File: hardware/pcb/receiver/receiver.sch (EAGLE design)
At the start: 78 parts, among them X1 5-1634506-1H

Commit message: hw: order list, receiver board schematic
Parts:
- added H1, H2, H3, H4: MOUNT-HOLE3.3, holes:MOUNT-HOLE3.3
- R7, R8, R9: MFR RC0805FR-0710KLRC0805FR-0710KL -> RC0805FR-0710KL
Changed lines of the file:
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@@
 <?xml version="1.0" encoding="utf-8"?>
 <!DOCTYPE eagle SYSTEM "eagle.dtd">
-<eagle version="7.5.0">
+<eagle version="7.3.0">
 <drawing>
 <settings>
@@
 <grid distance="0.1" unitdist="inch" unit="inch" style="lines" multiple="1" display="yes" altdistance="0.01" altunitdist="inch" altunit="inch"/>
 <layers>
-<layer number="1" name="Top" color="4" fill="1" visible="yes" active="no"/>
-<layer number="16" name="Bottom" color="1" fill="1" visible="yes" active="no"/>
-<layer number="17" name="Pads" color="2" fill="1" visible="yes" active="no"/>
-<layer number="18" name="Vias" color="2" fill="1" visible="yes" active="no"/>
-<layer number="19" name="Unrouted" color="6" fill="1" visible="yes" active="no"/>
-<layer number="20" name="Dimension" color="15" fill="1" visible="yes" active="no"/>
-<layer number="21" name="tPlace" color="7" fill="1" visible="yes" active="no"/>
-<layer number="22" name="bPlace" color="7" fill="1" visible="yes" active="no"/>
-<layer number="23" name="tOrigins" color="15" fill="1" visible="yes" active="no"/>
-<layer number="24" name="bOrigins" color="15" fill="1" visible="yes" active="no"/>
-<layer number="25" name="tNames" color="7" fill="1" visible="yes" active="no"/>
-<layer number="26" name="bNames" color="7" fill="1" visible="yes" active="no"/>
-<layer number="27" name="tValues" color="7" fill="1" visible="yes" active="no"/>
-<layer number="28" name="bValues" color="7" fill="1" visible="yes" active="no"/>
+<layer number="1" name="Top" color="4" fill="1" visible="no" active="no"/>
+<layer number="2" name="Route2" color="1" fill="3" visible="no" active="no"/>
+<layer number="3" name="Route3" color="4" fill="3" visible="no" active="no"/>
+<layer number="4" name="Route4" color="1" fill="4" visible="no" active="no"/>
+<layer number="5" name="Route5" color="4" fill="4" visible="no" active="no"/>
+<layer number="6" name="Route6" color="1" fill="8" visible="no" active="no"/>
+<layer number="7" name="Route7" color="4" fill="8" visible="no" active="no"/>
+<layer number="8" name="Route8" color="1" fill="2" visible="no" active="no"/>
+<layer number="9" name="Route9" color="4" fill="2" visible="no" active="no"/>
+<layer number="10" name="Route10" color="1" fill="7" visible="no" active="no"/>
+<layer number="11" name="Route11" color="4" fill="7" visible="no" active="no"/>
+<layer number="12" name="Route12" color="1" fill="5" visible="no" active="no"/>
+<layer number="13" name="Route13" color="4" fill="5" visible="no" active="no"/>
+<layer number="14" name="Route14" color="1" fill="6" visible="no" active="no"/>
+<layer number="15" name="Route15" color="4" fill="6" visible="no" active="no"/>
+<layer number="16" name="Bottom" color="1" fill="1" visible="no" active="no"/>
+<layer number="17" name="Pads" color="2" fill="1" visible="no" active="no"/>
+<layer number="18" name="Vias" color="2" fill="1" visible="no" active="no"/>
+<layer number="19" name="Unrouted" color="6" fill="1" visible="no" active="no"/>
+<layer number="20" name="Dimension" color="15" fill="1" visible="no" active="no"/>
+<layer number="21" name="tPlace" color="7" fill="1" visible="no" active="no"/>
+<layer number="22" name="bPlace" color="7" fill="1" visible="no" active="no"/>
+<layer number="23" name="tOrigins" color="15" fill="1" visible="no" active="no"/>
+<layer number="24" name="bOrigins" color="15" fill="1" visible="no" active="no"/>
+<layer number="25" name="tNames" color="7" fill="1" visible="no" active="no"/>
+<layer number="26" name="bNames" color="7" fill="1" visible="no" active="no"/>
+<layer number="27" name="tValues" color="7" fill="1" visible="no" active="no"/>
+<layer number="28" name="bValues" color="7" fill="1" visible="no" active="no"/>
 <layer number="29" name="tStop" color="7" fill="3" visible="no" active="no"/>
 <layer number="30" name="bStop" color="7" fill="6" visible="no" active="no"/>
@@
 <layer number="35" name="tGlue" color="7" fill="4" visible="no" active="no"/>
 <layer number="36" name="bGlue" color="7" fill="5" visible="no" active="no"/>
-<layer number="37" name="tTest" color="7" fill="1" visible="yes" active="no"/>
-<layer number="38" name="bTest" color="7" fill="1" visible="yes" active="no"/>
+<layer number="37" name="tTest" color="7" fill="1" visible="no" active="no"/>
+<layer number="38" name="bTest" color="7" fill="1" visible="no" active="no"/>
 <layer number="39" name="tKeepout" color="4" fill="11" visible="no" active="no"/>
 <layer number="40" name="bKeepout" color="1" fill="11" visible="no" active="no"/>
@@
 <layer number="44" name="Drills" color="7" fill="1" visible="no" active="no"/>
 <layer number="45" name="Holes" color="7" fill="1" visible="no" active="no"/>
-<layer number="46" name="Milling" color="3" fill="1" visible="yes" active="no"/>
-<layer number="47" name="Measures" color="7" fill="1" visible="yes" active="no"/>
-<layer number="48" name="Document" color="7" fill="1" visible="yes" active="no"/>
-<layer number="49" name="Reference" color="7" fill="1" visible="yes" active="no"/>
-<layer number="50" name="dxf" color="7" fill="1" visible="yes" active="no"/>
-<layer number="51" name="tDocu" color="7" fill="1" visible="yes" active="no"/>
-<layer number="52" name="bDocu" color="7" fill="1" visible="yes" active="no"/>
-<layer number="53" name="tGND_GNDA" color="7" fill="9" visible="yes" active="no"/>
-<layer number="54" name="bGND_GNDA" color="1" fill="9" visible="yes" active="no"/>
-<layer number="56" name="wert" color="7" fill="1" visible="yes" active="no"/>
-<layer number="57" name="tCAD" color="7" fill="1" visible="yes" active="no"/>
-<layer number="59" name="tCarbon" color="7" fill="1" visible="yes" active="no"/>
-<layer number="60" name="bCarbon" color="7" fill="1" visible="yes" active="no"/>
+<layer number="46" name="Milling" color="3" fill="1" visible="no" active="no"/>
+<layer number="47" name="Measures" color="7" fill="1" visible="no" active="no"/>
+<layer number="48" name="Document" color="7" fill="1" visible="no" active="no"/>
+<layer number="49" name="Reference" color="7" fill="1" visible="no" active="no"/>
+<layer number="50" name="dxf" color="7" fill="1" visible="no" active="no"/>
+<layer number="51" name="tDocu" color="7" fill="1" visible="no" active="no"/>
+<layer number="52" name="bDocu" color="7" fill="1" visible="no" active="no"/>
+<layer number="53" name="tGND_GNDA" color="7" fill="9" visible="no" active="no"/>
+<layer number="54" name="bGND_GNDA" color="1" fill="9" visible="no" active="no"/>
+<layer number="56" name="wert" color="7" fill="1" visible="no" active="no"/>
+<layer number="57" name="tCAD" color="7" fill="1" visible="no" active="no"/>
+<layer number="59" name="tCarbon" color="7" fill="1" visible="no" active="no"/>
+<layer number="60" name="bCarbon" color="7" fill="1" visible="no" active="no"/>
 <layer number="90" name="Modules" color="5" fill="1" visible="yes" active="yes"/>
 <layer number="91" name="Nets" color="2" fill="1" visible="yes" active="yes"/>
@@
 <part name="+3V5" library="supply1" deviceset="+3V3" device=""/>
 <part name="R7" library="rcl" deviceset="R-EU_" device="M0805" value="10k">
-<attribute name="MFR" value="RC0805FR-0710KLRC0805FR-0710KL"/>
+<attribute name="MFR" value="RC0805FR-0710KL"/>
 </part>
 <part name="JP1" library="lstolcman_thesis" deviceset="PINHD-2X4" device="">
@@
 </part>
 <part name="R8" library="rcl" deviceset="R-EU_" device="M0805" value="10k">
-<attribute name="MFR" value="RC0805FR-0710KLRC0805FR-0710KL"/>
+<attribute name="MFR" value="RC0805FR-0710KL"/>
 </part>
 <part name="R9" library="rcl" deviceset="R-EU_" device="M0805" value="10k">
-<attribute name="MFR" value="RC0805FR-0710KLRC0805FR-0710KL"/>
+<attribute name="MFR" value="RC0805FR-0710KL"/>
 </part>
 <part name="R12" library="rcl" deviceset="R-EU_" device="M0805" value="130R">
@@
 <attribute name="MFR" value="5-1634506-1"/>
 </part>
+<part name="H1" library="holes" deviceset="MOUNT-HOLE" device="3.3"/>
+<part name="H2" library="holes" deviceset="MOUNT-HOLE" device="3.3"/>
+<part name="H3" library="holes" deviceset="MOUNT-HOLE" device="3.3"/>
+<part name="H4" library="holes" deviceset="MOUNT-HOLE" device="3.3"/>
 </parts>
 <sheets>
@@
 <attribute name="MFR" x="-342.9" y="63.5" size="1.778" layer="96" display="off"/>
 </instance>
+<instance part="H1" gate="G$1" x="-340.36" y="10.16"/>
+<instance part="H2" gate="G$1" x="-340.36" y="2.54"/>
+<instance part="H3" gate="G$1" x="-340.36" y="-5.08"/>
+<instance part="H4" gate="G$1" x="-340.36" y="-12.7"/>
 </instances>
 <busses>

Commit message: hw: receiver board changes
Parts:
- removed C17, C23: 100n, rcl:C-EUC0805
- removed L6: ferrite bead, inductor-neosid:SM-NE29
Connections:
- removed net N$35: SV1.GPIO_00
- net +3V3: no longer C17.2, C42.2, JP1.1, L6.2, R11.2, R12.2, R7.2, V1.VCC
- net +3V3A_ADC: now also JP1.1, R11.2, R12.2, R7.2; no longer C23.2
- net AMPOUT_N: now also IC2.+OUT, R2.1; no longer IC2.-OUT, R1.1
- net AMPOUT_P: now also IC2.-OUT, R1.1; no longer IC2.+OUT, R2.1
- net ENC: now also SV1.GPIO_00; no longer SV1.GPIO_05
- net ENC_N: now also IC5.ENC_P; no longer IC5.ENC_N
- net ENC_P: now also IC5.ENC_N; no longer IC5.ENC_P
- net GND: no longer C17.1, C23.1
- net IN_N: now also IC5.AIN_N, R2.2; no longer IC5.AIN_P, R1.2
- net IN_P: now also IC5.AIN_P, R1.2; no longer IC5.AIN_N, R2.2
- net N$4: now also IC2.+IN; no longer IC2.-IN
- net N$5: now also IC2.-IN; no longer IC2.+IN
- net VDD: now also C42.2, V1.VCC; no longer L6.1
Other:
- moved on the sheet: C3, C38, C4, C5, R1, R2

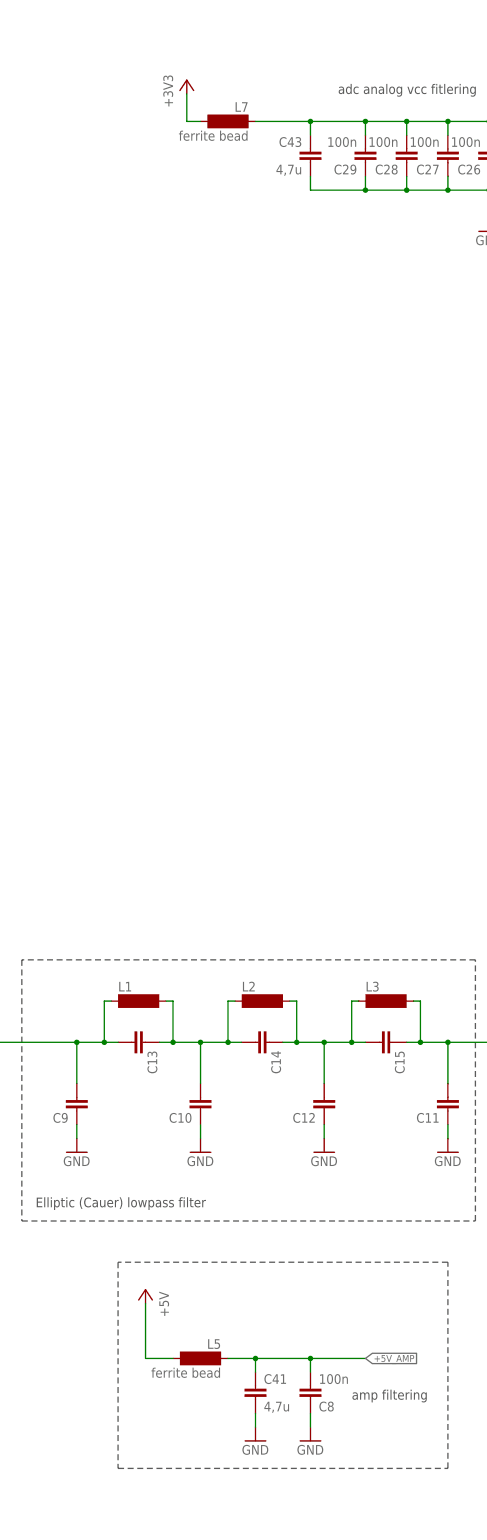
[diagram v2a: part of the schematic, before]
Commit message: hw: receiver ferrite beads between capacitors
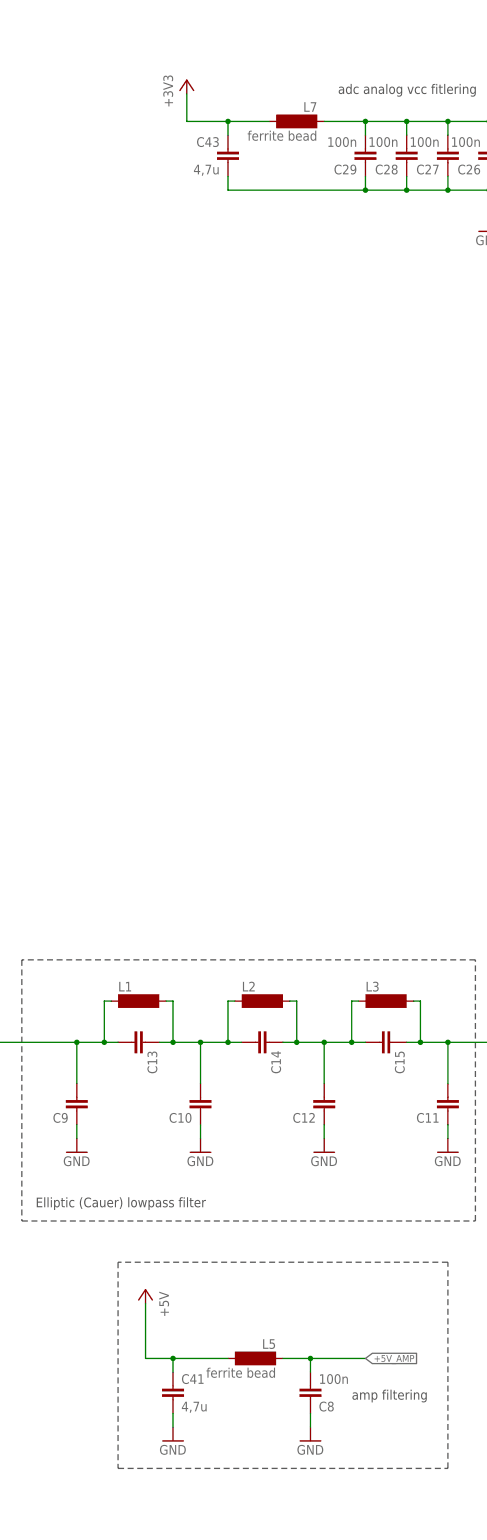
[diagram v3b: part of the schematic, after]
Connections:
- net +3V3: now also C43.1
- net +3V3A_ADC: no longer C43.1
- net +5V: now also C41.1
- net +5V_AMP: no longer C41.1
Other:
- moved on the sheet: C41, C43, L5, L7
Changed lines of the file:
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@@
 </instance>
 <instance part="GND19" gate="1" x="78.74" y="33.02"/>
-<instance part="L7" gate="G$1" x="-248.92" y="233.68" rot="MR0">
-<attribute name="MFR" x="-248.92" y="233.68" size="1.778" layer="96" rot="MR0" display="off"/>
+<instance part="L7" gate="G$1" x="-236.22" y="233.68" rot="MR0">
+<attribute name="MFR" x="-236.22" y="233.68" size="1.778" layer="96" rot="MR0" display="off"/>
 </instance>
 <instance part="C33" gate="G$1" x="147.32" y="43.18">
@@
 <attribute name="MFR" x="-53.34" y="223.52" size="1.778" layer="96" rot="MR0" display="off"/>
 </instance>
-<instance part="L5" gate="G$1" x="-254" y="5.08" rot="MR0">
-<attribute name="MFR" x="-254" y="5.08" size="1.778" layer="96" rot="MR0" display="off"/>
+<instance part="L5" gate="G$1" x="-243.84" y="5.08" rot="MR0">
+<attribute name="MFR" x="-243.84" y="5.08" size="1.778" layer="96" rot="MR0" display="off"/>
 </instance>
 <instance part="C34" gate="G$1" x="-233.68" y="276.86">
@@
 <attribute name="MFR" x="-109.22" y="213.36" size="2.54" layer="96" display="off"/>
 </instance>
-<instance part="C41" gate="G$1" x="-243.84" y="0">
-<attribute name="MFR" x="-243.84" y="0" size="2.54" layer="96" display="off"/>
-</instance>
-<instance part="GND31" gate="1" x="-243.84" y="-10.16"/>
+<instance part="C41" gate="G$1" x="-259.08" y="0">
+<attribute name="MFR" x="-259.08" y="0" size="2.54" layer="96" display="off"/>
+</instance>
+<instance part="GND31" gate="1" x="-259.08" y="-10.16"/>
 <instance part="C42" gate="G$1" x="73.66" y="-15.24" rot="R180">
 <attribute name="MFR" x="73.66" y="-15.24" size="2.54" layer="96" rot="R180" display="off"/>
@@
 <instance part="GND32" gate="1" x="73.66" y="-22.86"/>
 <instance part="+3V4" gate="G$1" x="-256.54" y="241.3"/>
-<instance part="C43" gate="G$1" x="-233.68" y="228.6" rot="MR0">
-<attribute name="MFR" x="-233.68" y="228.6" size="2.54" layer="96" rot="MR0" display="off"/>
+<instance part="C43" gate="G$1" x="-248.92" y="228.6" rot="MR0">
+<attribute name="MFR" x="-248.92" y="228.6" size="2.54" layer="96" rot="MR0" display="off"/>
 </instance>
 <instance part="+3V1" gate="G$1" x="-43.18" y="233.68"/>
@@
 <pinref part="C29" gate="G$1" pin="1"/>
 <pinref part="C43" gate="G$1" pin="2"/>
-<wire x1="-233.68" y1="220.98" x2="-233.68" y2="223.52" width="0.1524" layer="91"/>
-<wire x1="-233.68" y1="220.98" x2="-223.52" y2="220.98" width="0.1524" layer="91"/>
+<wire x1="-223.52" y1="220.98" x2="-248.92" y2="220.98" width="0.1524" layer="91"/>
+<wire x1="-248.92" y1="220.98" x2="-248.92" y2="223.52" width="0.1524" layer="91"/>
 <junction x="-223.52" y="220.98"/>
 </segment>
@@
 <segment>
 <pinref part="C41" gate="G$1" pin="2"/>
-<wire x1="-243.84" y1="-5.08" x2="-243.84" y2="-7.62" width="0.1524" layer="91"/>
+<wire x1="-259.08" y1="-5.08" x2="-259.08" y2="-7.62" width="0.1524" layer="91"/>
 <pinref part="GND31" gate="1" pin="GND"/>
 </segment>
@@
 <segment>
 <pinref part="L7" gate="G$1" pin="2"/>
-<wire x1="-254" y1="233.68" x2="-256.54" y2="233.68" width="0.1524" layer="91"/>
+<wire x1="-241.3" y1="233.68" x2="-248.92" y2="233.68" width="0.1524" layer="91"/>
+<wire x1="-248.92" y1="233.68" x2="-256.54" y2="233.68" width="0.1524" layer="91"/>
 <wire x1="-256.54" y1="233.68" x2="-256.54" y2="238.76" width="0.1524" layer="91"/>
 <pinref part="+3V4" gate="G$1" pin="+3V3"/>
+<pinref part="C43" gate="G$1" pin="1"/>
+<wire x1="-248.92" y1="231.14" x2="-248.92" y2="233.68" width="0.1524" layer="91"/>
+<junction x="-248.92" y="233.68"/>
 </segment>
 </net>
@@
 <pinref part="C29" gate="G$1" pin="2"/>
 <pinref part="L7" gate="G$1" pin="1"/>
-<wire x1="-223.52" y1="233.68" x2="-233.68" y2="233.68" width="0.1524" layer="91"/>
-<wire x1="-233.68" y1="233.68" x2="-243.84" y2="233.68" width="0.1524" layer="91"/>
+<wire x1="-223.52" y1="233.68" x2="-231.14" y2="233.68" width="0.1524" layer="91"/>
 <junction x="-223.52" y="233.68"/>
-<pinref part="C43" gate="G$1" pin="1"/>
-<wire x1="-233.68" y1="231.14" x2="-233.68" y2="233.68" width="0.1524" layer="91"/>
-<junction x="-233.68" y="233.68"/>
 <wire x1="-200.66" y1="233.68" x2="-200.66" y2="238.76" width="0.1524" layer="91"/>
 <wire x1="-200.66" y1="238.76" x2="-193.04" y2="238.76" width="0.1524" layer="91"/>
@@
 <net name="+5V_AMP" class="0">
 <segment>
-<wire x1="-248.92" y1="5.08" x2="-243.84" y2="5.08" width="0.1524" layer="91"/>
 <label x="-223.52" y="5.08" size="1.27" layer="95" xref="yes"/>
-<wire x1="-243.84" y1="5.08" x2="-233.68" y2="5.08" width="0.1524" layer="91"/>
+<wire x1="-238.76" y1="5.08" x2="-233.68" y2="5.08" width="0.1524" layer="91"/>
 <wire x1="-233.68" y1="5.08" x2="-223.52" y2="5.08" width="0.1524" layer="91"/>
 <wire x1="-233.68" y1="2.54" x2="-233.68" y2="5.08" width="0.1524" layer="91"/>
@@
 <pinref part="C8" gate="G$1" pin="2"/>
 <pinref part="L5" gate="G$1" pin="1"/>
-<pinref part="C41" gate="G$1" pin="1"/>
-<wire x1="-243.84" y1="2.54" x2="-243.84" y2="5.08" width="0.1524" layer="91"/>
-<junction x="-243.84" y="5.08"/>
 </segment>
 <segment>
@@
 <wire x1="-264.16" y1="5.08" x2="-264.16" y2="15.24" width="0.1524" layer="91"/>
 <pinref part="P+1" gate="1" pin="+5V"/>
+<wire x1="-248.92" y1="5.08" x2="-259.08" y2="5.08" width="0.1524" layer="91"/>
+<pinref part="L5" gate="G$1" pin="2"/>
+<pinref part="C41" gate="G$1" pin="1"/>
 <wire x1="-259.08" y1="5.08" x2="-264.16" y2="5.08" width="0.1524" layer="91"/>
-<pinref part="L5" gate="G$1" pin="2"/>
-</segment>
-</net>
+<wire x1="-259.08" y1="2.54" x2="-259.08" y2="5.08" width="0.1524" layer="91"/>
+<junction x="-259.08" y="5.08"/>
+</segment>
+</net>

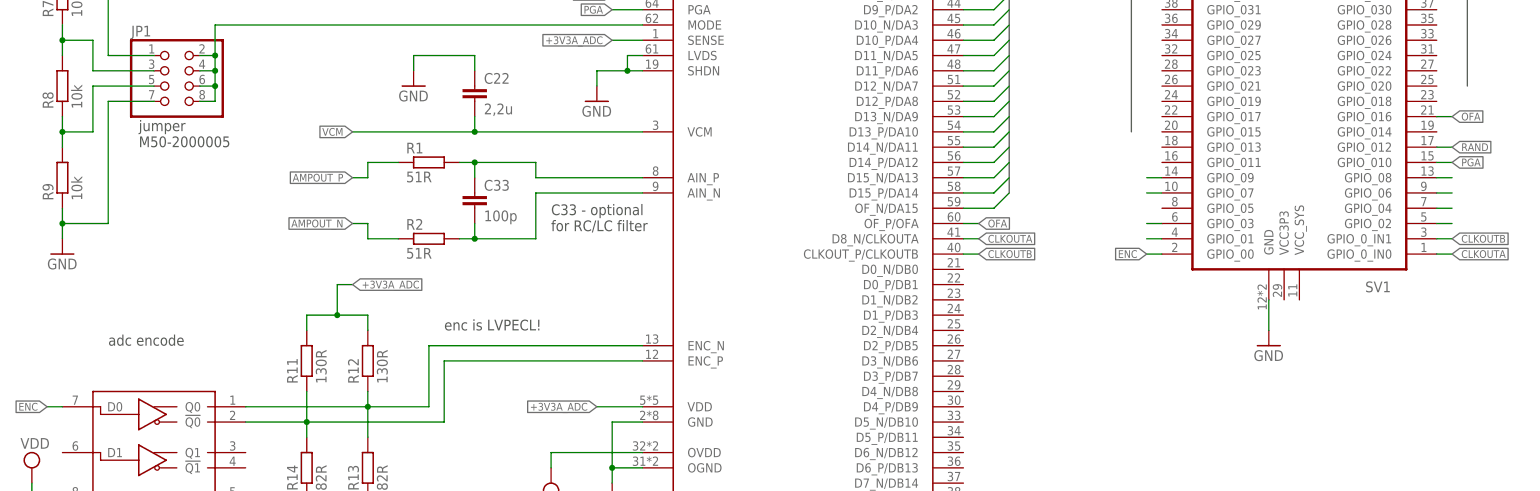
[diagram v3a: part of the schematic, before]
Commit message: hw: modified adc input clock resistors resistors
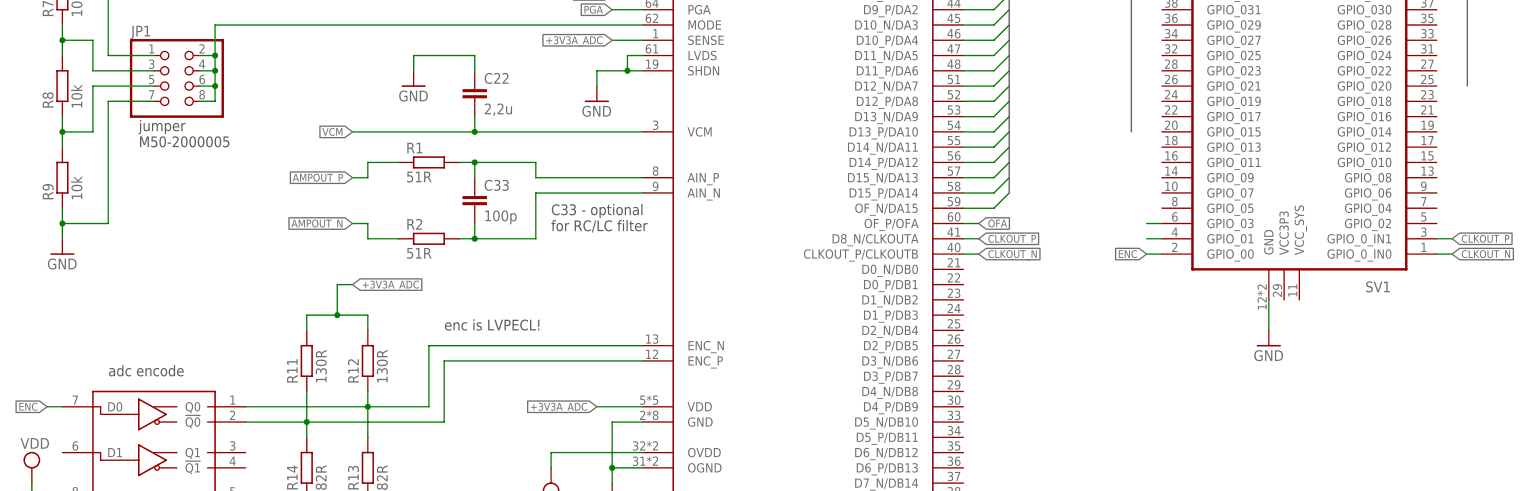
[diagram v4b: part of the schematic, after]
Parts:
- R11, R12: device rcl:R-EU_M0805 -> rcl:R-EU_M1206; MFR RC0805FR-07130RL -> ERJ-8ENF1300V
- R13, R14: device rcl:R-EU_M0805 -> rcl:R-EU_M1206; MFR RC0805FR-0782RL -> RC1206JR-0782RL
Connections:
- removed net CLKOUTA: IC5.D8_N/CLKOUTA, SV1.GPIO_0_IN0
- removed net CLKOUTB: IC5.CLKOUT_P/CLKOUTB, SV1.GPIO_0_IN1
- removed net N$10: SV1.GPIO_09
- removed net N$11: SV1.GPIO_07
- removed net N$24: SV1.GPIO_08
- removed net N$26: SV1.GPIO_06
- removed net N$29: SV1.GPIO_04
- removed net N$30: SV1.GPIO_02
- new net CLKOUT_N: IC5.CLKOUT_P/CLKOUTB, SV1.GPIO_0_IN0
- new net CLKOUT_P: IC5.D8_N/CLKOUTA, SV1.GPIO_0_IN1
- net OFA: no longer SV1.GPIO_016
- net PGA: no longer SV1.GPIO_010
- net RAND: no longer SV1.GPIO_012
